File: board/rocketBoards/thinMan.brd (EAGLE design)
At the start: 45 x 16 mm, 54 parts, among them J1 47346-0001

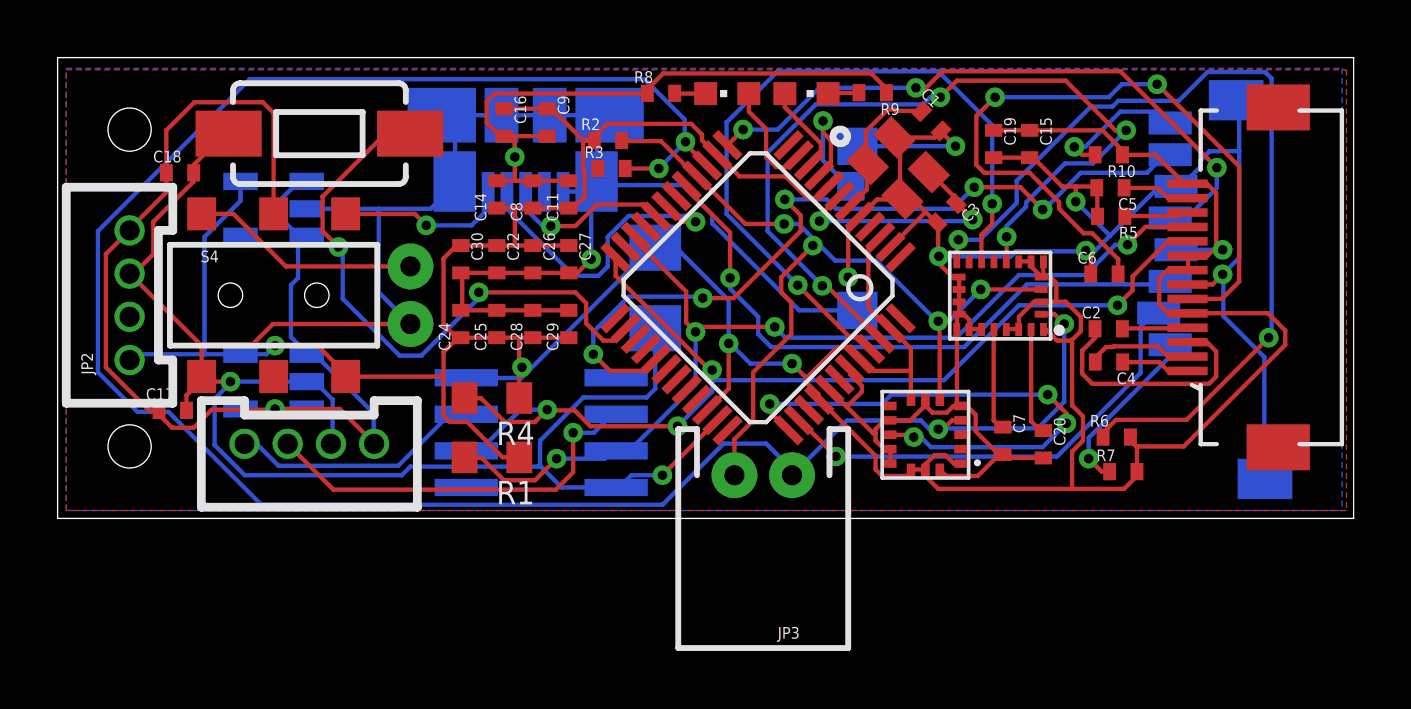
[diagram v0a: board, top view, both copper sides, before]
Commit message: Routed all. Fixed USB connectivity Issue; Pending Crystal check up/power checkup
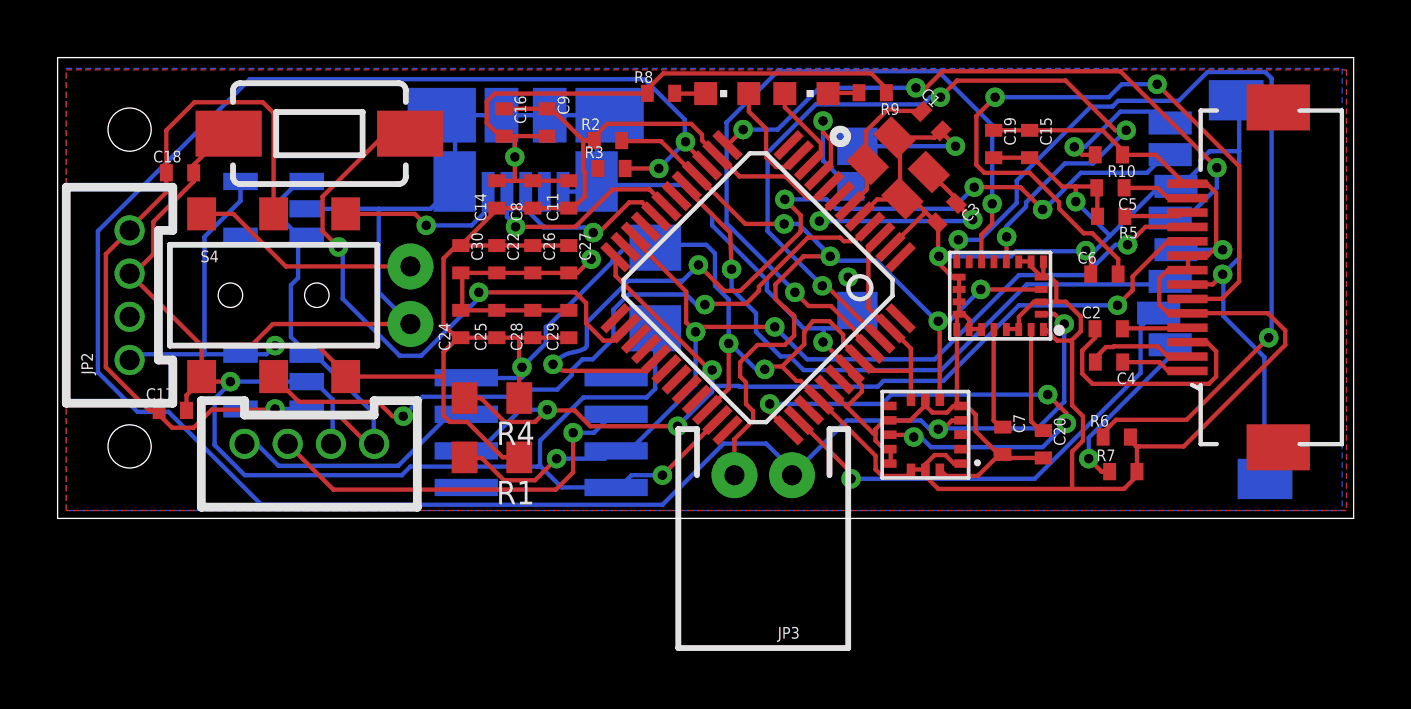
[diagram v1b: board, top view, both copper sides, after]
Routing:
- net PIO0_1: track 0.00 -> 25.2 mm, vias 0 -> 2
- net 3.3V: track 147.5 -> 152.0 mm
- net N$17: track 10.9 -> 7.35 mm
- net SSP1_MISO: track 28.3 -> 31.7 mm
- net I2C0_SDA: track 29.9 -> 32.1 mm
- net GND: track 202.8 -> 200.9 mm, vias 10 -> 11
- net SSP1_SSEL: track 16.0 -> 16.8 mm
- net SSP1_MOSI: track 21.6 -> 22.3 mm
- net I2C1_SDA: track 34.8 -> 35.4 mm
